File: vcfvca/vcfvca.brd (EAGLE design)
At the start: 160 x 50.5 mm, 106 parts, among them IC1 LM13700N, IC2 LM4558N, IC3 LM13700N, IC4 LM13700N, IC5 LM4558N, J1 POWER, J2 FREQ, J3 RES, J4 AMP, J5 AUD_IN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

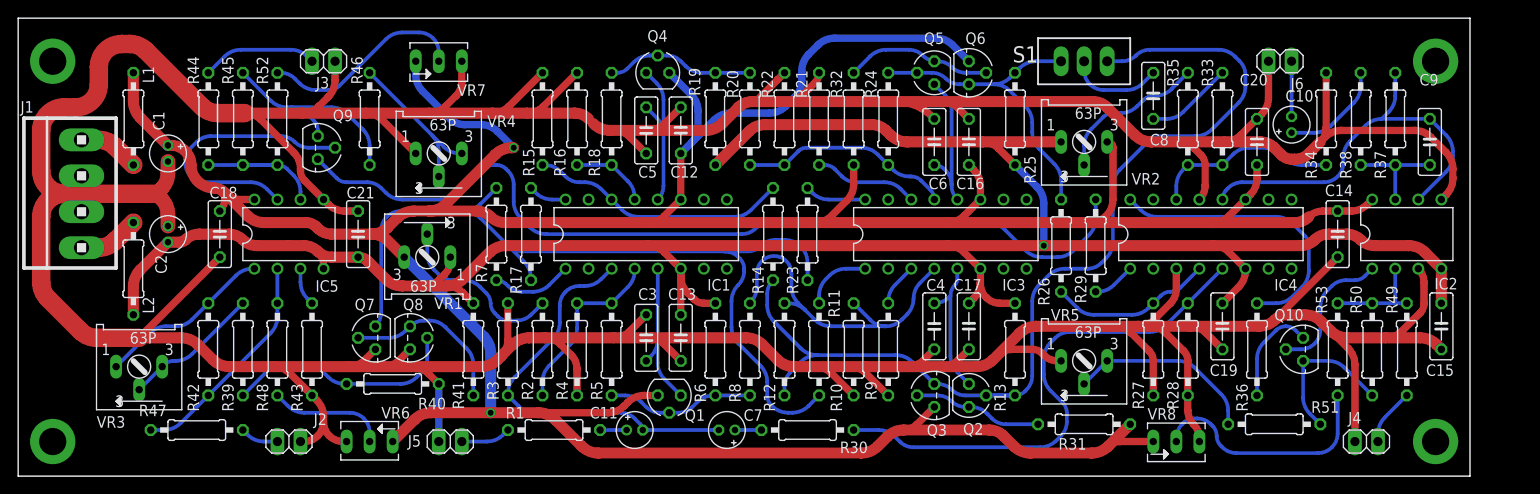
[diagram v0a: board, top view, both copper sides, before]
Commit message: Move PCB to 0,0
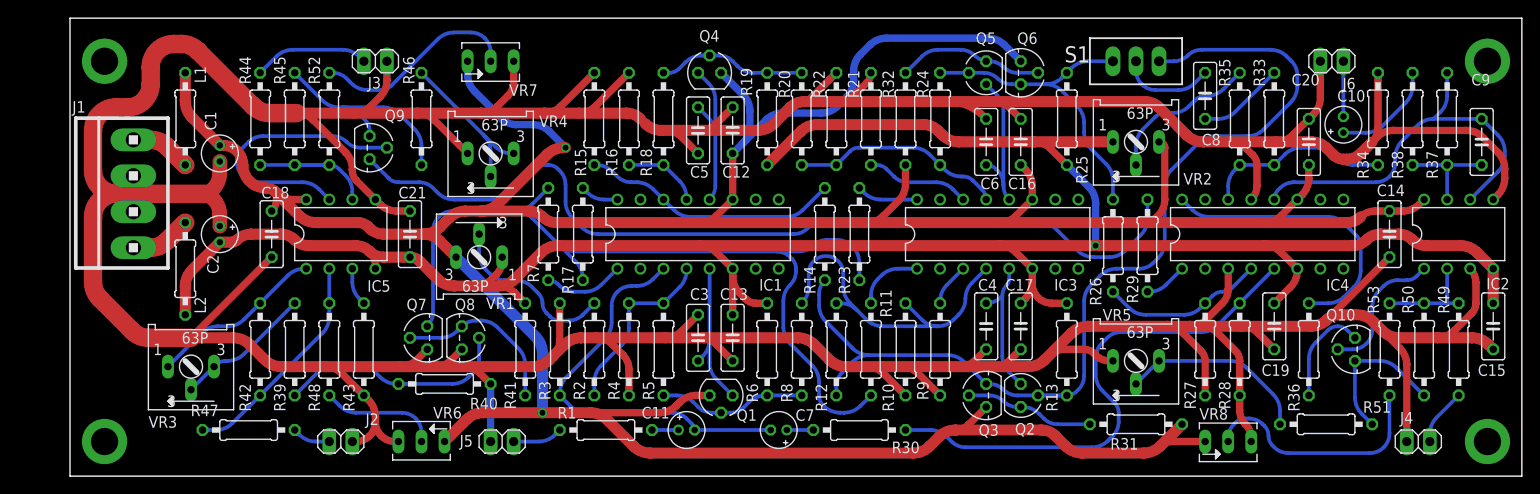
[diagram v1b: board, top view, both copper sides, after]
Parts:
- moved C10 5.72 mm to (140.3, 38.7)
- moved C12 5.72 mm to (73.0, 38.1)
- moved C13 5.72 mm to (73.0, 15.2)
- moved C14 5.72 mm to (145.4, 26.7)
- moved C15 5.72 mm to (156.8, 16.5)
- moved C16 5.72 mm to (104.8, 36.8)
- moved C17 5.72 mm to (104.8, 16.5)
- moved C19 5.72 mm to (132.7, 16.5)
- moved C20 5.72 mm to (136.5, 36.8)
- moved C21 5.72 mm to (37.5, 26.7)
- moved C3 5.72 mm to (69.2, 15.2)
- moved C4 5.72 mm to (101.0, 16.5)
- moved C5 5.72 mm to (69.2, 38.1)
- moved C6 5.72 mm to (101.0, 36.8)
- moved C7 5.72 mm to (78.1, 5.08)
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
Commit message: VCF/VCA: revision for final submission
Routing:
- net -15V: track 275.0 -> 276.4 mm
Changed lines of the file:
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@@
 <dimension x1="0" y1="0" x2="160.02" y2="0" x3="80.01" y3="-6.35" textsize="1.778" layer="51"/>
 <text x="36.195" y="0.254" size="1.778" layer="27">FREQ</text>
-<text x="48.133" y="49.784" size="1.778" layer="27" rot="SR180">RES</text>
+<text x="48.133" y="49.657" size="1.778" layer="27" rot="SR180">RES</text>
 <text x="125.349" y="0.254" size="1.778" layer="27" rot="SR0">AMP</text>
 <text x="66.04" y="49.657" size="1.27" layer="51" rot="SR180">ACMS Spring 2020
@@
 <text x="95.377" y="49.657" size="1.27" layer="51" rot="SR180">KENOBI (based on OB-1)
 4-pole VCF and VCA</text>
-<text x="5.715" y="45.085" size="1.778" layer="51" rot="SR270">+15</text>
-<text x="5.715" y="21.59" size="1.778" layer="51" rot="SR270">-15</text>
+<text x="7.62" y="45.085" size="1.778" layer="51" rot="SR270">+15</text>
+<text x="7.62" y="21.59" size="1.778" layer="51" rot="SR270">-15</text>
 <text x="11.176" y="30.226" size="1.778" layer="51" rot="SR0">GND</text>
 <dimension x1="0" y1="50.47" x2="0" y2="0" x3="-6.35" y3="25.235" textsize="1.778" layer="51"/>
+<text x="44.196" y="1.016" size="1.016" layer="51">GND</text>
+<text x="30.861" y="1.016" size="1.016" layer="51">GND</text>
+<text x="145.034" y="1.016" size="1.016" layer="51">GND</text>
+<text x="138.049" y="48.895" size="1.016" layer="51" rot="SR180">GND</text>
+<text x="37.084" y="48.895" size="1.016" layer="51" rot="SR180">GND</text>
 </plain>
 <attributes>
@@
 <attribute name="POPULARITY" value="12" x="200.025" y="108.585" size="1.778" layer="27" rot="R90" display="off"/>
 <attribute name="SPICEPREFIX" value="C" x="200.025" y="108.585" size="1.778" layer="27" rot="R90" display="off"/>
-<attribute name="VALUE" x="142.748" y="44.577" size="1.27" layer="27" ratio="10" rot="R180"/>
+<attribute name="VALUE" x="141.478" y="36.322" size="1.27" layer="27" ratio="10" rot="R180"/>
 </element>
 <element name="C11" library="rcl" library_urn="urn:adsk.eagle:library:334" package="E1,8-4" package3d_urn="urn:adsk.eagle:package:23336/2" value="6u8" x="67.945" y="5.08" smashed="yes">
@@
 </element>
 <element name="C9" library="rcl" library_urn="urn:adsk.eagle:library:334" package="C050-025X075" package3d_urn="urn:adsk.eagle:package:23637/1" value="300p" x="155.575" y="36.83" smashed="yes" rot="R270">
-<attribute name="NAME" x="154.432" y="43.053" size="1.27" layer="25" ratio="10"/>
+<attribute name="NAME" x="154.432" y="41.148" size="1.27" layer="25" ratio="10"/>
 <attribute name="POPULARITY" value="29" x="116.205" y="-20.32" size="1.778" layer="27" rot="R270" display="off"/>
 <attribute name="SPICEPREFIX" value="C" x="116.205" y="-20.32" size="1.778" layer="27" rot="R270" display="off"/>
-<attribute name="VALUE" x="153.67" y="41.148" size="1.27" layer="27" ratio="10"/>
+<attribute name="VALUE" x="158.242" y="34.925" size="1.27" layer="27" ratio="10" rot="R90"/>
 </element>
 <element name="IC1" library="national-semiconductor" library_urn="urn:adsk.eagle:library:307" package="DIL16" package3d_urn="urn:adsk.eagle:package:21232/1" value="LM13700N" x="69.215" y="26.67" smashed="yes">
@@
 </element>
 <element name="J6" library="pinhead" library_urn="urn:adsk.eagle:library:325" package="1X02" package3d_urn="urn:adsk.eagle:package:22435/2" value="AUD_OUT" x="139.065" y="45.72" smashed="yes" rot="R180">
-<attribute name="NAME" x="141.6812" y="43.8912" size="1.27" layer="25" ratio="10" rot="R180"/>
+<attribute name="NAME" x="142.1638" y="45.6438" size="1.27" layer="25" ratio="10"/>
 <attribute name="POPULARITY" value="98" x="81.915" y="74.93" size="1.778" layer="27" rot="R180" display="off"/>
-<attribute name="VALUE" x="149.987" y="49.784" size="1.778" layer="27" rot="SR180"/>
+<attribute name="VALUE" x="149.987" y="49.657" size="1.778" layer="27" rot="SR180"/>
 </element>
 <element name="Q1" library="transistor-small-signal" library_urn="urn:adsk.eagle:library:401" package="SOT54C" package3d_urn="urn:adsk.eagle:package:29742/3" value="BF245" x="71.755" y="8.89" smashed="yes" rot="R180">
@@
 </element>
 <element name="R47" library="rcl" library_urn="urn:adsk.eagle:library:334" package="0207/10" package3d_urn="urn:adsk.eagle:package:23491/2" value="100k 1%" x="19.685" y="5.08" smashed="yes" rot="R180">
-<attribute name="NAME" x="16.383" y="7.874" size="1.27" layer="25" ratio="10" rot="R180"/>
+<attribute name="NAME" x="15.748" y="4.064" size="1.27" layer="25" ratio="10" rot="R180"/>
 <attribute name="POPULARITY" value="36" x="-50.165" y="100.33" size="1.778" layer="27" rot="R180" display="off"/>
 <attribute name="SPICEPREFIX" value="R" x="-50.165" y="100.33" size="1.778" layer="27" rot="R180" display="off"/>
@@
 </element>
 <element name="S1" library="switch" library_urn="urn:adsk.eagle:library:380" package="TL3XPO" package3d_urn="urn:adsk.eagle:package:27745/1" value="12dB/24dB" x="117.475" y="45.72" smashed="yes">
-<attribute name="NAME" x="109.601" y="45.593" size="1.778" layer="25"/>
+<attribute name="NAME" x="122.936" y="46.228" size="1.27" layer="25"/>
 <attribute name="POPULARITY" value="2" x="207.645" y="39.37" size="1.778" layer="27" display="off"/>
 <attribute name="VALUE" x="123.825" y="49.911" size="1.778" layer="27" rot="SR180"/>
@@
 <wire x1="31.486975" y1="25.4" x2="26.298025" y2="25.4" width="1.2192" layer="1"/>
 <wire x1="31.486975" y1="25.4" x2="33.02" y2="24.765" width="1.2192" layer="1" curve="-45"/>
-<wire x1="33.02" y1="24.765" x2="34.553025" y2="24.13" width="1.2192" layer="1" curve="45"/>
-<wire x1="34.553025" y1="24.13" x2="37.465" y2="24.13" width="1.2192" layer="1"/>
-<wire x1="37.465" y1="24.13" x2="38.5490125" y2="23.6809875" width="1.2192" layer="1" curve="-45"/>
-<wire x1="40.53105" y1="21.69895" x2="42.327103125" y2="20.955" width="1.2192" layer="1" curve="45"/>
-<wire x1="42.327103125" y1="20.955" x2="47.207896875" y2="20.955" width="1.2192" layer="1"/>
-<wire x1="38.5490125" y1="23.6809875" x2="40.53105" y2="21.69895" width="1.2192" layer="1"/>
+<wire x1="43.18" y1="20.955" x2="47.207896875" y2="20.955" width="1.2192" layer="1"/>
 <wire x1="47.207896875" y1="20.955" x2="49.00395" y2="21.69895" width="1.2192" layer="1" curve="45"/>
 <wire x1="51.96105" y1="24.65605" x2="53.757103125" y2="25.4" width="1.2192" layer="1" curve="-45"/>
@@
 <wire x1="46.99" y1="22.225" x2="46.46395" y2="21.69895" width="0.8128" layer="1"/>
 <wire x1="46.46395" y1="21.69895" x2="44.667896875" y2="20.955" width="0.8128" layer="1" curve="-45"/>
-<wire x1="44.667896875" y1="20.955" x2="42.327103125" y2="20.955" width="0.8128" layer="1"/>
+<wire x1="44.667896875" y1="20.955" x2="43.18" y2="20.955" width="0.8128" layer="1"/>
 <wire x1="76.835" y1="34.29" x2="80.53605" y2="37.99105" width="1.2192" layer="1"/>
 <wire x1="80.53605" y1="37.99105" x2="82.332103125" y2="38.735" width="1.2192" layer="1" curve="-45"/>
@@
 <wire x1="23.231975" y1="26.67" x2="24.765" y2="26.035" width="1.2192" layer="1" curve="-45"/>
 <wire x1="19.948025" y1="26.67" x2="23.231975" y2="26.67" width="1.2192" layer="1"/>
+<wire x1="33.02" y1="24.765" x2="33.2059875" y2="24.5790125" width="1.2192" layer="1"/>
+<wire x1="33.2059875" y1="24.5790125" x2="34.29" y2="24.13" width="1.2192" layer="1" curve="45"/>
+<wire x1="34.29" y1="24.13" x2="35.3740125" y2="23.6809875" width="1.2192" layer="1" curve="-45"/>
+<wire x1="35.3740125" y1="23.6809875" x2="37.35605" y2="21.69895" width="1.2192" layer="1"/>
+<wire x1="37.35605" y1="21.69895" x2="39.152103125" y2="20.955" width="1.2192" layer="1" curve="45"/>
+<wire x1="39.152103125" y1="20.955" x2="43.18" y2="20.955" width="1.2192" layer="1"/>
+<wire x1="37.465" y1="24.13" x2="36.3809875" y2="23.6809875" width="0.8128" layer="1" curve="-45"/>
+<wire x1="36.3809875" y1="23.6809875" x2="35.3740125" y2="23.6809875" width="0.8128" layer="1"/>
 </signal>
 <signal name="N$2">
@@
 <contactref element="VR1" pad="S"/>
 <wire x1="56.515" y1="17.78" x2="57.785" y2="19.05" width="0.4064" layer="16"/>
-<wire x1="45.085" y1="26.67" x2="45.085" y2="24.547103125" width="0.4064" layer="16"/>
-<wire x1="45.085" y1="24.547103125" x2="45.82895" y2="22.75105" width="0.4064" layer="16" curve="45"/>
-<wire x1="45.82895" y1="22.75105" x2="46.355" y2="22.225" width="0.4064" layer="16"/>
-<wire x1="46.355" y1="22.225" x2="47.888025" y2="21.59" width="0.4064" layer="16" curve="45"/>
-<wire x1="49.112896875" y1="21.59" x2="50.90895" y2="20.84605" width="0.4064" layer="16" curve="-45"/>
-<wire x1="51.6209875" y1="20.1340125" x2="52.07" y2="19.05" width="0.4064" layer="16" curve="-45"/>
+<wire x1="52.07" y1="19.05" x2="51.6209875" y2="20.1340125" width="0.4064" layer="16" curve="45"/>
 <wire x1="52.07" y1="19.05" x2="52.5190125" y2="17.9659875" width="0.4064" layer="16" curve="45"/>
 <wire x1="52.8909875" y1="17.5940125" x2="53.975" y2="17.145" width="0.4064" layer="16" curve="45"/>
 <wire x1="53.975" y1="17.145" x2="54.981975" y2="17.145" width="0.4064" layer="16"/>
 <wire x1="54.981975" y1="17.145" x2="56.515" y2="17.78" width="0.4064" layer="16" curve="45"/>
-<wire x1="47.888025" y1="21.59" x2="49.112896875" y2="21.59" width="0.4064" layer="16"/>
-<wire x1="50.90895" y1="20.84605" x2="51.6209875" y2="20.1340125" width="0.4064" layer="16"/>
 <wire x1="52.5190125" y1="17.9659875" x2="52.8909875" y2="17.5940125" width="0.4064" layer="16"/>
+<wire x1="51.6209875" y1="20.1340125" x2="50.90895" y2="20.84605" width="0.4064" layer="16"/>
+<wire x1="50.90895" y1="20.84605" x2="50.165" y2="22.642103125" width="0.4064" layer="16" curve="-45"/>
+<wire x1="50.165" y1="24.501975" x2="49.53" y2="26.035" width="0.4064" layer="16" curve="45"/>
+<wire x1="49.53" y1="26.035" x2="47.996975" y2="26.67" width="0.4064" layer="16" curve="45"/>
+<wire x1="47.996975" y1="26.67" x2="45.085" y2="26.67" width="0.4064" layer="16"/>
+<wire x1="50.165" y1="22.642103125" x2="50.165" y2="24.501975" width="0.4064" layer="16"/>
 </signal>
 <signal name="N$37">
